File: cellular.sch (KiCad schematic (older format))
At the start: 3 parts

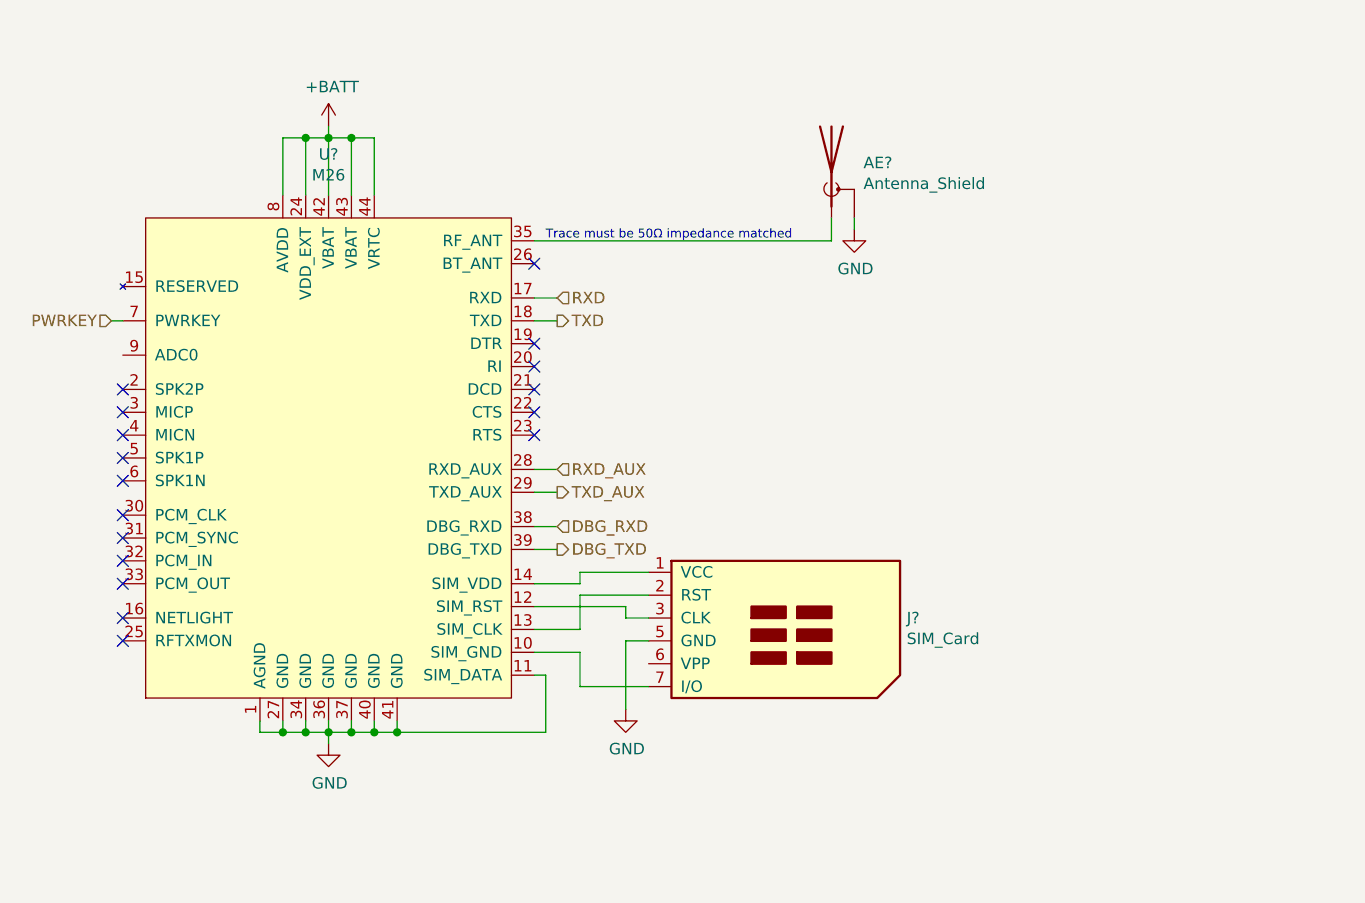
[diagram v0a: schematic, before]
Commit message: lots of improvements to schematic: fixing decoupling, matching reference designs and recommendations better, connecting pins to esp32 and adding i2c gpio expander
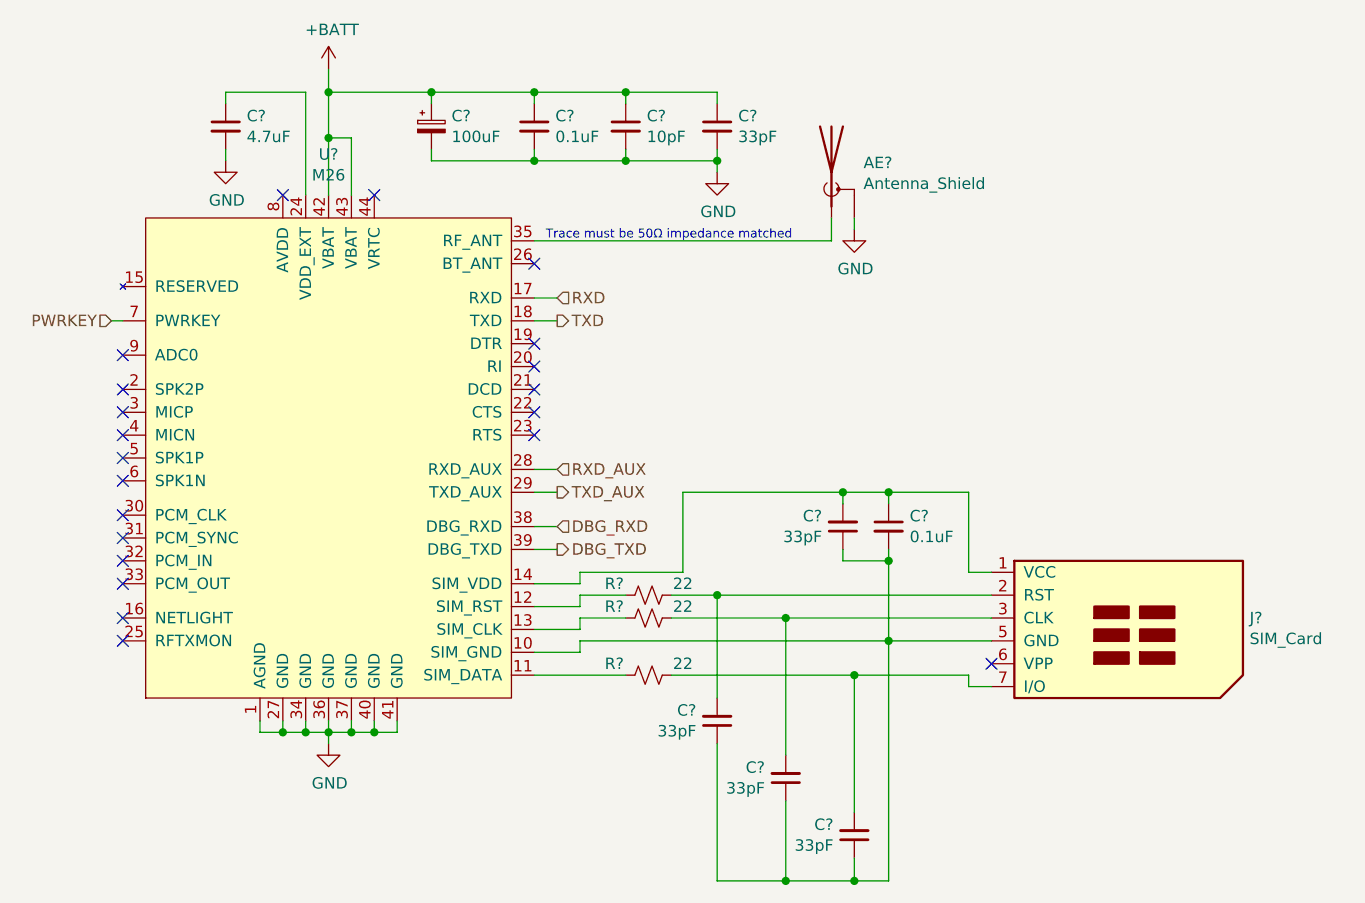
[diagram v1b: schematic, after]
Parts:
- added C?: 4.7uF, symbol Device:C_Small
- added C? (x2): 0.1uF, symbol Device:C_Small
- added C? (x5): 33pF, symbol Device:C_Small
- added C?: 100uF, symbol Device:CP_Small
- added C?: 10pF, symbol Device:C_Small
- added R? (x3): 22, symbol Device:R_Small_US
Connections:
- net +BATT: now also C?.1, C?.1, C?.1, C?.1; no longer U?.24 (VDD_EXT), U?.44 (VRTC), U?.8 (AVDD)
- net GND: now also C?.2, C?.2, C?.2, C?.2, C?.2; no longer J?.5 (GND), U?.11 (SIM_DATA)
- net at U?.10 (SIM_GND): now also J?.5 (GND), C?.1, C?.1, C?.1, C?.1, C?.2; no longer J?.7 (I/O)
- net at U?.12 (SIM_RST): now also R?.2; no longer J?.3 (CLK)
- net at U?.13 (SIM_CLK): now also R?.2; no longer J?.2 (RST)
- net at J?.1 (VCC), U?.14 (SIM_VDD): now also C?.1, C?.2
- new net: R?.2, U?.11 (SIM_DATA)
- new net: C?.1, U?.24 (VDD_EXT)
- new net: C?.2, J?.2 (RST), R?.1
- new net: C?.2, J?.3 (CLK), R?.1
- new net: C?.2, J?.7 (I/O), R?.1
- no-connect marks 17 -> 21
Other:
- moved on the sheet: J?

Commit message: annotate schematic
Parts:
- gave numbers to parts that had none: 16
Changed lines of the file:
@@
 $EndDescr
 $Comp
-L thingb:M26 U?
+L thingb:M26 U10
 U 1 1 5C9AECA6
 P 2250 2550
-F 0 "U?" H 2250 3878 50  0000 C CNN
+F 0 "U10" H 2250 3878 50  0000 C CNN
 F 1 "M26" H 2250 3787 50  0000 C CNN
 F 2 "" H 2250 2550 50  0001 C CNN
@@
 NoConn ~ 1350 2650
 $Comp
-L Device:Antenna_Shield AE?
+L Device:Antenna_Shield AE1
 U 1 1 5C9AEE16
 P 4450 1300
-F 0 "AE?" H 4590 1341 50  0000 L CNN
+F 0 "AE1" H 4590 1341 50  0000 L CNN
 F 1 "Antenna_Shield" H 4590 1250 50  0000 L CNN
 F 2 "Connector_Coaxial:U.FL_Molex_MCRF_73412-0110_Vertical" H 4450 1400 50  0001 C CNN
@@
 	4450 1600 4450 1500
 $Comp
-L power:GND #PWR?
+L power:GND #PWR052
 U 1 1 5C9AEED4
 P 4550 1550
-F 0 "#PWR?" H 4550 1300 50  0001 C CNN
+F 0 "#PWR052" H 4550 1300 50  0001 C CNN
 F 1 "GND" H 4555 1377 50  0000 C CNN
 F 2 "" H 4550 1550 50  0001 C CNN
@@
 NoConn ~ 1350 3250
 $Comp
-L power:GND #PWR?
+L power:GND #PWR050
 U 1 1 5C9B042C
 P 2250 3800
-F 0 "#PWR?" H 2250 3550 50  0001 C CNN
+F 0 "#PWR050" H 2250 3550 50  0001 C CNN
 F 1 "GND" H 2255 3627 50  0000 C CNN
 F 2 "" H 2250 3800 50  0001 C CNN
@@
 	2250 3750 2250 3800
 $Comp
-L Connector:SIM_Card J?
+L Connector:SIM_Card J4
 U 1 1 5C9B0C92
 P 5650 3350
-F 0 "J?" H 6279 3450 50  0000 L CNN
+F 0 "J4" H 6279 3450 50  0000 L CNN
 F 1 "SIM_Card" H 6279 3359 50  0000 L CNN
 F 2 "" H 5650 3700 50  0001 C CNN
@@
 	2350 1150 2250 1150
 $Comp
-L power:+BATT #PWR?
+L power:+BATT #PWR049
 U 1 1 5CA67C60
 P 2250 850
-F 0 "#PWR?" H 2250 700 50  0001 C CNN
+F 0 "#PWR049" H 2250 700 50  0001 C CNN
 F 1 "+BATT" H 2265 1023 50  0000 C CNN
 F 2 "" H 2250 850 50  0001 C CNN
@@
 NoConn ~ 2050 1400
 $Comp
-L Device:C_Small C?
+L Device:C_Small C15
 U 1 1 5D5D7303
 P 1800 1100
-F 0 "C?" H 1892 1146 50  0000 L CNN
+F 0 "C15" H 1892 1146 50  0000 L CNN
 F 1 "4.7uF" H 1892 1055 50  0000 L CNN
 F 2 "" H 1800 1100 50  0001 C CNN
@@
 $EndComp
 $Comp
-L power:GND #PWR?
+L power:GND #PWR048
 U 1 1 5D5D9D65
 P 1800 1250
-F 0 "#PWR?" H 1800 1000 50  0001 C CNN
+F 0 "#PWR048" H 1800 1000 50  0001 C CNN
 F 1 "GND" H 1805 1077 50  0000 C CNN
 F 2 "" H 1800 1250 50  0001 C CNN
@@
 	1800 950  1800 1000
 $Comp
-L Device:C_Small C?
+L Device:C_Small C24
 U 1 1 5D5DD206
 P 4700 2850
-F 0 "C?" H 4792 2896 50  0000 L CNN
+F 0 "C24" H 4792 2896 50  0000 L CNN
 F 1 "0.1uF" H 4792 2805 50  0000 L CNN
 F 2 "" H 4700 2850 50  0001 C CNN
@@
 NoConn ~ 5150 3450
 $Comp
-L Device:R_Small_US R?
+L Device:R_Small_US R16
 U 1 1 5D5E2ECB
 P 3650 3150
-F 0 "R?" V 3600 3000 50  0000 C CNN
+F 0 "R16" V 3600 3000 50  0000 C CNN
 F 1 "22" V 3600 3300 50  0000 C CNN
 F 2 "" H 3650 3150 50  0001 C CNN
@@
 	3750 3150 3950 3150
 $Comp
-L Device:R_Small_US R?
+L Device:R_Small_US R17
 U 1 1 5D5E8317
 P 3650 3250
-F 0 "R?" V 3600 3100 50  0000 C CNN
+F 0 "R17" V 3600 3100 50  0000 C CNN
 F 1 "22" V 3600 3400 50  0000 C CNN
 F 2 "" H 3650 3250 50  0001 C CNN
@@
 Connection ~ 4700 2700
 $Comp
-L Device:R_Small_US R?
+L Device:R_Small_US R18
 U 1 1 5D5F3F1B
 P 3650 3500
-F 0 "R?" V 3600 3350 50  0000 C CNN
+F 0 "R18" V 3600 3350 50  0000 C CNN
 F 1 "22" V 3600 3650 50  0000 C CNN
 F 2 "" H 3650 3500 50  0001 C CNN
@@
 	5050 3500 4550 3500
 $Comp
-L Device:C_Small C?
+L Device:C_Small C22
 U 1 1 5D5F7DFB
 P 4500 2850
-F 0 "C?" H 4409 2804 50  0000 R CNN
+F 0 "C22" H 4409 2804 50  0000 R CNN
 F 1 "33pF" H 4409 2895 50  0000 R CNN
 F 2 "" H 4500 2850 50  0001 C CNN
@@
 	4500 2700 4700 2700
 $Comp
-L Device:C_Small C?
+L Device:C_Small C20
 U 1 1 5D5FC3FC
 P 3950 3700
-F 0 "C?" H 3859 3654 50  0000 R CNN
+F 0 "C20" H 3859 3654 50  0000 R CNN
 F 1 "33pF" H 3859 3745 50  0000 R CNN
 F 2 "" H 3950 3700 50  0001 C CNN
@@
 	3950 3150 5150 3150
 $Comp
-L Device:C_Small C?
+L Device:C_Small C21
 U 1 1 5D5FDAEC
 P 4250 3950
-F 0 "C?" H 4159 3904 50  0000 R CNN
+F 0 "C21" H 4159 3904 50  0000 R CNN
 F 1 "33pF" H 4159 3995 50  0000 R CNN
 F 2 "" H 4250 3950 50  0001 C CNN
@@
 	3150 3500 3550 3500
 $Comp
-L Device:C_Small C?
+L Device:C_Small C23
 U 1 1 5D60FB3C
 P 4550 4200
-F 0 "C?" H 4459 4154 50  0000 R CNN
+F 0 "C23" H 4459 4154 50  0000 R CNN
 F 1 "33pF" H 4459 4245 50  0000 R CNN
 F 2 "" H 4550 4200 50  0001 C CNN
@@
 Connection ~ 4250 4400
 $Comp
-L Device:CP_Small C?
+L Device:CP_Small C16
 U 1 1 5D622E7F
 P 2700 1100
-F 0 "C?" H 2788 1146 50  0000 L CNN
+F 0 "C16" H 2788 1146 50  0000 L CNN
 F 1 "100uF" H 2788 1055 50  0000 L CNN
 F 2 "" H 2700 1100 50  0001 C CNN
@@
 $EndComp
 $Comp
-L Device:C_Small C?
+L Device:C_Small C17
 U 1 1 5D623741
 P 3150 1100
-F 0 "C?" H 3242 1146 50  0000 L CNN
+F 0 "C17" H 3242 1146 50  0000 L CNN
 F 1 "0.1uF" H 3242 1055 50  0000 L CNN
 F 2 "" H 3150 1100 50  0001 C CNN
@@
 $EndComp
 $Comp
-L Device:C_Small C?
+L Device:C_Small C18
 U 1 1 5D626C11
 P 3550 1100
-F 0 "C?" H 3642 1146 50  0000 L CNN
+F 0 "C18" H 3642 1146 50  0000 L CNN
 F 1 "10pF" H 3642 1055 50  0000 L CNN
 F 2 "" H 3550 1100 50  0001 C CNN
@@
 $EndComp
 $Comp
-L Device:C_Small C?
+L Device:C_Small C19
 U 1 1 5D627055
 P 3950 1100
-F 0 "C?" H 4042 1146 50  0000 L CNN
+F 0 "C19" H 4042 1146 50  0000 L CNN
 F 1 "33pF" H 4042 1055 50  0000 L CNN
 F 2 "" H 3950 1100 50  0001 C CNN
@@
 	3550 1250 3150 1250
 $Comp
-L power:GND #PWR?
+L power:GND #PWR051
 U 1 1 5D634214
 P 3950 1300
-F 0 "#PWR?" H 3950 1050 50  0001 C CNN
+F 0 "#PWR051" H 3950 1050 50  0001 C CNN
 F 1 "GND" H 3955 1127 50  0000 C CNN
 F 2 "" H 3950 1300 50  0001 C CNN

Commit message: reannotate schematic
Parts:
- renumbered R16 to R17, R17 to R18, R18 to R19
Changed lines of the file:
@@
 	4450 1600 4450 1500
 $Comp
-L power:GND #PWR050
+L power:GND #PWR051
 U 1 1 5C9AEED4
 P 4550 1550
-F 0 "#PWR050" H 4550 1300 50  0001 C CNN
+F 0 "#PWR051" H 4550 1300 50  0001 C CNN
 F 1 "GND" H 4555 1377 50  0000 C CNN
 F 2 "" H 4550 1550 50  0001 C CNN
@@
 NoConn ~ 1350 3250
 $Comp
-L power:GND #PWR048
+L power:GND #PWR049
 U 1 1 5C9B042C
 P 2250 3800
-F 0 "#PWR048" H 2250 3550 50  0001 C CNN
+F 0 "#PWR049" H 2250 3550 50  0001 C CNN
 F 1 "GND" H 2255 3627 50  0000 C CNN
 F 2 "" H 2250 3800 50  0001 C CNN
@@
 	2350 1150 2250 1150
 $Comp
-L power:+BATT #PWR047
+L power:+BATT #PWR048
 U 1 1 5CA67C60
 P 2250 850
-F 0 "#PWR047" H 2250 700 50  0001 C CNN
+F 0 "#PWR048" H 2250 700 50  0001 C CNN
 F 1 "+BATT" H 2265 1023 50  0000 C CNN
 F 2 "" H 2250 850 50  0001 C CNN
@@
 $EndComp
 $Comp
-L power:GND #PWR046
+L power:GND #PWR047
 U 1 1 5D5D9D65
 P 1800 1250
-F 0 "#PWR046" H 1800 1000 50  0001 C CNN
+F 0 "#PWR047" H 1800 1000 50  0001 C CNN
 F 1 "GND" H 1805 1077 50  0000 C CNN
 F 2 "" H 1800 1250 50  0001 C CNN
@@
 NoConn ~ 5150 3450
 $Comp
-L Device:R_Small_US R16
+L Device:R_Small_US R17
 U 1 1 5D5E2ECB
 P 3650 3150
-F 0 "R16" V 3600 3000 50  0000 C CNN
+F 0 "R17" V 3600 3000 50  0000 C CNN
 F 1 "22" V 3600 3300 50  0000 C CNN
 F 2 "" H 3650 3150 50  0001 C CNN
@@
 	3750 3150 3950 3150
 $Comp
-L Device:R_Small_US R17
+L Device:R_Small_US R18
 U 1 1 5D5E8317
 P 3650 3250
-F 0 "R17" V 3600 3100 50  0000 C CNN
+F 0 "R18" V 3600 3100 50  0000 C CNN
 F 1 "22" V 3600 3400 50  0000 C CNN
 F 2 "" H 3650 3250 50  0001 C CNN
@@
 Connection ~ 4700 2700
 $Comp
-L Device:R_Small_US R18
+L Device:R_Small_US R19
 U 1 1 5D5F3F1B
 P 3650 3500
-F 0 "R18" V 3600 3350 50  0000 C CNN
+F 0 "R19" V 3600 3350 50  0000 C CNN
 F 1 "22" V 3600 3650 50  0000 C CNN
 F 2 "" H 3650 3500 50  0001 C CNN
@@
 	3550 1250 3150 1250
 $Comp
-L power:GND #PWR049
+L power:GND #PWR050
 U 1 1 5D634214
 P 3950 1300
-F 0 "#PWR049" H 3950 1050 50  0001 C CNN
+F 0 "#PWR050" H 3950 1050 50  0001 C CNN
 F 1 "GND" H 3955 1127 50  0000 C CNN
 F 2 "" H 3950 1300 50  0001 C CNN

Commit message: associate footprints with all parts
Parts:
- C15, C17, C18, C19, C20, C21, C22, C23, C24: footprint (none) -> Capacitor_SMD:C_0603_1608Metric_Pad1.05x0.95mm_HandSolder
- C16: footprint (none) -> Capacitor_Tantalum_SMD:CP_EIA-3528-15_AVX-H_Pad1.50x2.35mm_HandSolder
- J4: footprint (none) -> thingb:7112S0815X19LF
- R17, R18, R19: footprint (none) -> Resistor_SMD:R_0603_1608Metric_Pad1.05x0.95mm_HandSolder
- U10: footprint (none) -> thingb:M26
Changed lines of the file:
@@
 F 0 "U10" H 2250 3878 50  0000 C CNN
 F 1 "M26" H 2250 3787 50  0000 C CNN
-F 2 "" H 2250 2550 50  0001 C CNN
+F 2 "thingb:M26" H 2250 2550 50  0001 C CNN
 F 3 "https://fccid.io/XMR201604M26/User-Manual/Users-Manual-3010753.pdf" H 2250 2550 50  0001 C CNN
 	1    2250 2550
@@
 F 0 "J4" H 6279 3450 50  0000 L CNN
 F 1 "SIM_Card" H 6279 3359 50  0000 L CNN
-F 2 "" H 5650 3700 50  0001 C CNN
+F 2 "thingb:7112S0815X19LF" H 5650 3700 50  0001 C CNN
 F 3 " ~" H 5600 3350 50  0001 C CNN
 	1    5650 3350
@@
 F 0 "C15" H 1892 1146 50  0000 L CNN
 F 1 "4.7uF" H 1892 1055 50  0000 L CNN
-F 2 "" H 1800 1100 50  0001 C CNN
+F 2 "Capacitor_SMD:C_0603_1608Metric_Pad1.05x0.95mm_HandSolder" H 1800 1100 50  0001 C CNN
 F 3 "~" H 1800 1100 50  0001 C CNN
 	1    1800 1100
@@
 F 0 "C24" H 4792 2896 50  0000 L CNN
 F 1 "0.1uF" H 4792 2805 50  0000 L CNN
-F 2 "" H 4700 2850 50  0001 C CNN
+F 2 "Capacitor_SMD:C_0603_1608Metric_Pad1.05x0.95mm_HandSolder" H 4700 2850 50  0001 C CNN
 F 3 "~" H 4700 2850 50  0001 C CNN
 	1    4700 2850
@@
 F 0 "R17" V 3600 3000 50  0000 C CNN
 F 1 "22" V 3600 3300 50  0000 C CNN
-F 2 "" H 3650 3150 50  0001 C CNN
+F 2 "Resistor_SMD:R_0603_1608Metric_Pad1.05x0.95mm_HandSolder" H 3650 3150 50  0001 C CNN
 F 3 "~" H 3650 3150 50  0001 C CNN
 	1    3650 3150
@@
 F 0 "R18" V 3600 3100 50  0000 C CNN
 F 1 "22" V 3600 3400 50  0000 C CNN
-F 2 "" H 3650 3250 50  0001 C CNN
+F 2 "Resistor_SMD:R_0603_1608Metric_Pad1.05x0.95mm_HandSolder" H 3650 3250 50  0001 C CNN
 F 3 "~" H 3650 3250 50  0001 C CNN
 	1    3650 3250
@@
 F 0 "R19" V 3600 3350 50  0000 C CNN
 F 1 "22" V 3600 3650 50  0000 C CNN
-F 2 "" H 3650 3500 50  0001 C CNN
+F 2 "Resistor_SMD:R_0603_1608Metric_Pad1.05x0.95mm_HandSolder" H 3650 3500 50  0001 C CNN
 F 3 "~" H 3650 3500 50  0001 C CNN
 	1    3650 3500
@@
 F 0 "C22" H 4409 2804 50  0000 R CNN
 F 1 "33pF" H 4409 2895 50  0000 R CNN
-F 2 "" H 4500 2850 50  0001 C CNN
+F 2 "Capacitor_SMD:C_0603_1608Metric_Pad1.05x0.95mm_HandSolder" H 4500 2850 50  0001 C CNN
 F 3 "~" H 4500 2850 50  0001 C CNN
 	1    4500 2850
@@
 F 0 "C20" H 3859 3654 50  0000 R CNN
 F 1 "33pF" H 3859 3745 50  0000 R CNN
-F 2 "" H 3950 3700 50  0001 C CNN
+F 2 "Capacitor_SMD:C_0603_1608Metric_Pad1.05x0.95mm_HandSolder" H 3950 3700 50  0001 C CNN
 F 3 "~" H 3950 3700 50  0001 C CNN
 	1    3950 3700
@@
 F 0 "C21" H 4159 3904 50  0000 R CNN
 F 1 "33pF" H 4159 3995 50  0000 R CNN
-F 2 "" H 4250 3950 50  0001 C CNN
+F 2 "Capacitor_SMD:C_0603_1608Metric_Pad1.05x0.95mm_HandSolder" H 4250 3950 50  0001 C CNN
 F 3 "~" H 4250 3950 50  0001 C CNN
 	1    4250 3950
@@
 F 0 "C23" H 4459 4154 50  0000 R CNN
 F 1 "33pF" H 4459 4245 50  0000 R CNN
-F 2 "" H 4550 4200 50  0001 C CNN
+F 2 "Capacitor_SMD:C_0603_1608Metric_Pad1.05x0.95mm_HandSolder" H 4550 4200 50  0001 C CNN
 F 3 "~" H 4550 4200 50  0001 C CNN
 	1    4550 4200
@@
 F 0 "C16" H 2788 1146 50  0000 L CNN
 F 1 "100uF" H 2788 1055 50  0000 L CNN
-F 2 "" H 2700 1100 50  0001 C CNN
+F 2 "Capacitor_Tantalum_SMD:CP_EIA-3528-15_AVX-H_Pad1.50x2.35mm_HandSolder" H 2700 1100 50  0001 C CNN
 F 3 "~" H 2700 1100 50  0001 C CNN
 	1    2700 1100
@@
 F 0 "C17" H 3242 1146 50  0000 L CNN
 F 1 "0.1uF" H 3242 1055 50  0000 L CNN
-F 2 "" H 3150 1100 50  0001 C CNN
+F 2 "Capacitor_SMD:C_0603_1608Metric_Pad1.05x0.95mm_HandSolder" H 3150 1100 50  0001 C CNN
 F 3 "~" H 3150 1100 50  0001 C CNN
 	1    3150 1100
@@
 F 0 "C18" H 3642 1146 50  0000 L CNN
 F 1 "10pF" H 3642 1055 50  0000 L CNN
-F 2 "" H 3550 1100 50  0001 C CNN
+F 2 "Capacitor_SMD:C_0603_1608Metric_Pad1.05x0.95mm_HandSolder" H 3550 1100 50  0001 C CNN
 F 3 "~" H 3550 1100 50  0001 C CNN
 	1    3550 1100
@@
 F 0 "C19" H 4042 1146 50  0000 L CNN
 F 1 "33pF" H 4042 1055 50  0000 L CNN
-F 2 "" H 3950 1100 50  0001 C CNN
+F 2 "Capacitor_SMD:C_0603_1608Metric_Pad1.05x0.95mm_HandSolder" H 3950 1100 50  0001 C CNN
 F 3 "~" H 3950 1100 50  0001 C CNN
 	1    3950 1100
